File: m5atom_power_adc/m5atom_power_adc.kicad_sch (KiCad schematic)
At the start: 125 parts, among them J1 Conn_01x04_Socket, J10 Relay2, J11 R0SW, J12 R1SW, J13 R2SW, J14 Conn_01x02, J2 GROVE-CONNECTOR, J3 Conn_01x04_Pin, J4 USB_C_Receptacle_USB2.0_16P, J5 SubBatt, J6 MainBatt, J7 Relay0, J8 Relay1, J9 GROVE-CONNECTOR, Q1 AO3401A, Q2 MMBT2222A, Q3 MMBT2222A, Q4 MMBT2222A, Q5 AO3401A, Q6 MMBT2222A, Q7 MMBT2222A, Q8 AO3401A, Q9 MMBT2222A, SW1 Boot, SW2 Reset, U1 LM2596S-5, U2 ESP32-S3-MINI-1, U3 AMS1117-3.3, U4 ADS1115IDGS, U5 AMS1117-3.3, U6 LTC2944

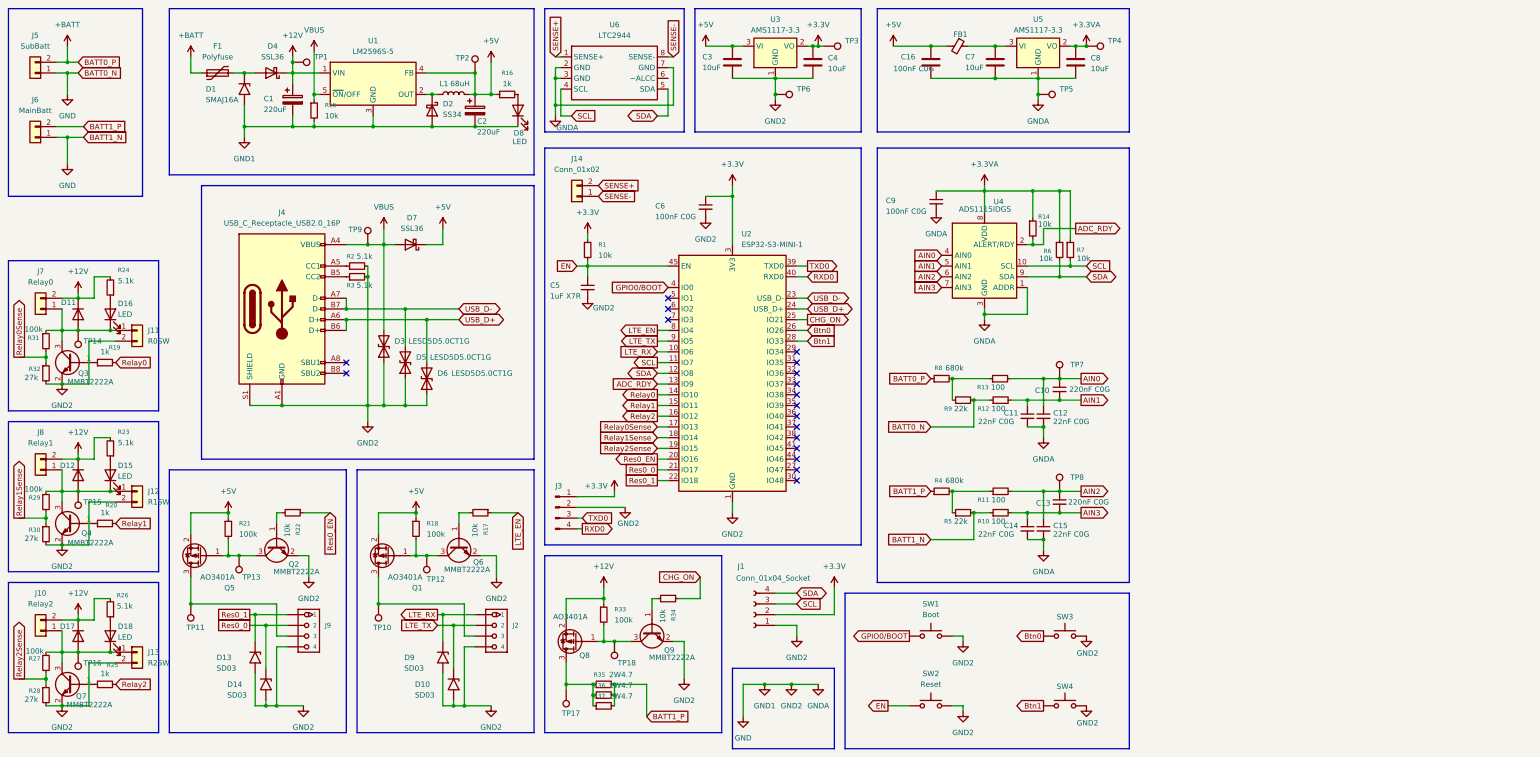
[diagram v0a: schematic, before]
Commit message: refactor: 回路図をフラットから階層化に移行、ブザー回路追加
- 回路図: フラット構成から階層シート構成へ移行（共通回路の共通化）
  - メインシート（1xx）: 電源・ESP32・ADC・ブザー等トップレベル
  - RelayControl サブシート: リレードライバ回路（Q×2、D×3、R×6）
  - VoltageSense サブシート: 電圧分圧回路（C×4、R×5）
  - GroveUnit サブシート: Grove 電源スイッチ回路（Q×3、D×3、R×3）
- 回路図: リファレンス番号をページ番号+xx体系に変更
- 回路図: ブザー回路追加（LS101/MLT-8530 + Q103/AO3401A ハイサイドスイッチ、GPIO34）
- HARDWARE.md: ブザー回路仕様を追記（駆動条件・部品表）
- HARDWARE.md: 赤色LED選定（XL-1608SURC-06）追記
- HARDWARE.md: 電源系統別トレース幅・ビアサイズ表を拡充
- HARDWARE.md: LM2596スイッチングノードの配線注意事項を追記

Co-Authored-By: Claude Sonnet 4.6 <noreply@anthropic.com>
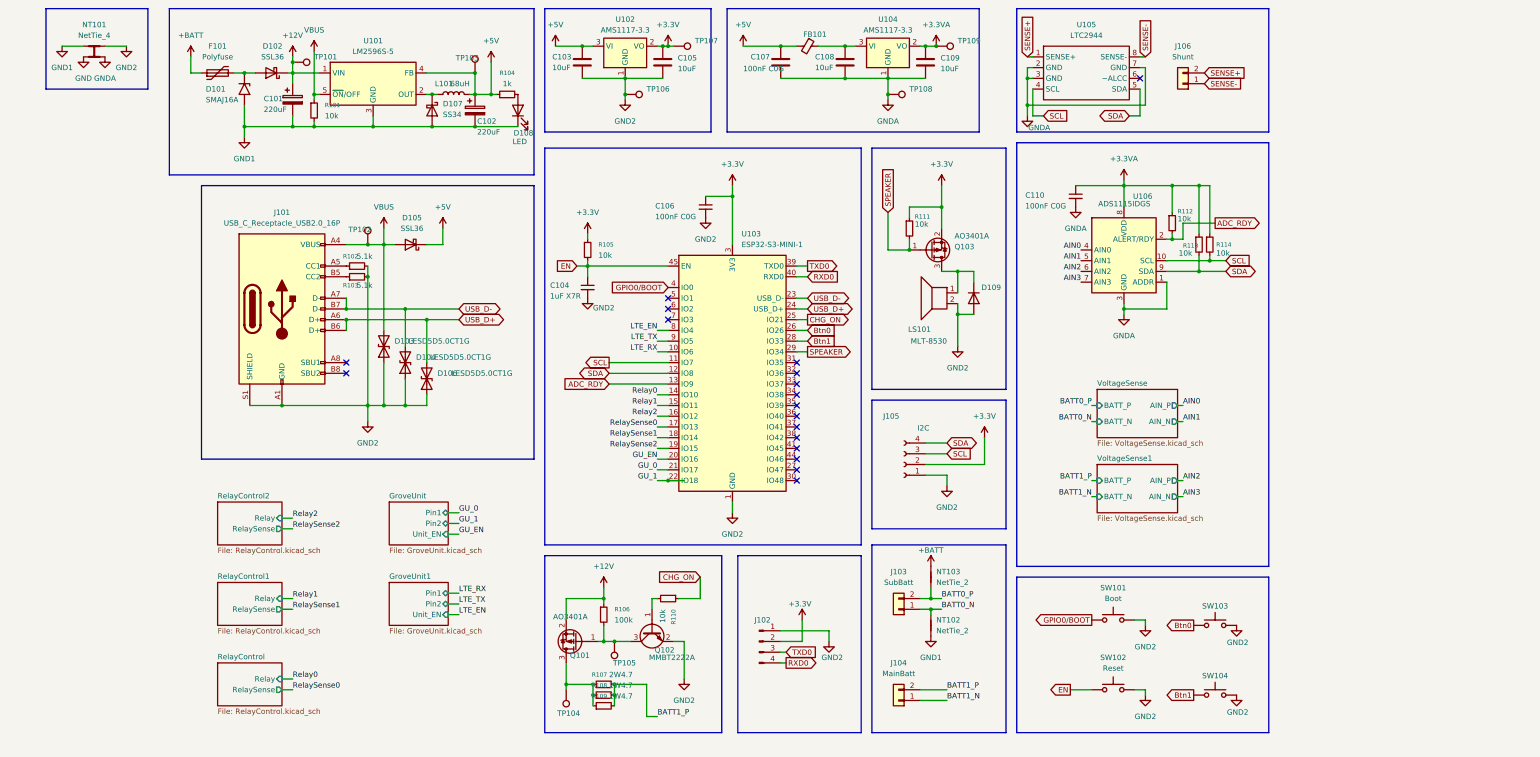
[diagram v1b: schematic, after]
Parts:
- removed C10, C13: 220nF C0G, Capacitor_SMD:C_1206_3216Metric, symbol Device:C_Small
- removed C11, C12, C14, C15: 22nF C0G, Capacitor_SMD:C_0805_2012Metric, symbol Device:C_Small
- removed D10, D13, D14, D9: SD03, Diode_SMD:D_SOD-323, symbol Diode:SMAJ16A
- removed D11, D12, D17: 1N4148WS, Diode_SMD:D_SOD-323, symbol Diode:1N4148WS
- removed D15, D16, D18: LED, LED_SMD:LED_0603_1608Metric, symbol Device:LED
- removed J10: Relay2, Connector_JST:JST_XH_B2B-XH-A_1x02_P2.50mm_Vertical, symbol Connector_Generic:Conn_01x02
- removed J11: R0SW, Connector_JST:JST_XH_B2B-XH-A_1x02_P2.50mm_Vertical, symbol Connector_Generic:Conn_01x02
- removed J12: R1SW, Connector_JST:JST_XH_B2B-XH-A_1x02_P2.50mm_Vertical, symbol Connector_Generic:Conn_01x02
- removed J13: R2SW, Connector_JST:JST_XH_B2B-XH-A_1x02_P2.50mm_Vertical, symbol Connector_Generic:Conn_01x02
- removed J2, J9: GROVE-CONNECTOR, 000_Local:HY2.0-4PWB, symbol OPL_Connector:GROVE-CONNECTOR-DIP_4P-2.0_
- removed J7: Relay0, Connector_JST:JST_XH_B2B-XH-A_1x02_P2.50mm_Vertical, symbol Connector_Generic:Conn_01x02
- removed J8: Relay1, Connector_JST:JST_XH_B2B-XH-A_1x02_P2.50mm_Vertical, symbol Connector_Generic:Conn_01x02
- removed Q1, Q5: AO3401A, Package_TO_SOT_SMD:SOT-23, symbol Transistor_FET:AO3401A
- removed Q2, Q3, Q4, Q6, Q7: MMBT2222A, Package_TO_SOT_SMD:SOT-23, symbol Transistor_BJT:MMBT2222A
- removed R10, R11, R12, R13: 100, Resistor_SMD:R_0402_1005Metric, symbol Device:R_Small
- removed R17, R22: 10k, Resistor_SMD:R_0402_1005Metric, symbol Device:R_Small
- removed R18, R21, R27, R29, R31: 100k, Resistor_SMD:R_0603_1608Metric, symbol Device:R_Small
- removed R19, R20, R25: 1k, Resistor_SMD:R_0603_1608Metric, symbol Device:R_Small
- removed R23, R24, R26: 5.1k, Resistor_SMD:R_0603_1608Metric, symbol Device:R_Small
- removed R28, R30, R32: 27k, Resistor_SMD:R_0603_1608Metric, symbol Device:R_Small
- removed R4, R8: 680k, Resistor_SMD:R_0603_1608Metric, symbol Device:R_Small
- removed R5, R9: 22k, Resistor_SMD:R_0402_1005Metric, symbol Device:R_Small
- removed TP10, TP11, TP12, TP13, TP14, TP15, TP16, TP7, TP8: TestPoint, TestPoint:TestPoint_Pad_D1.5mm, symbol Connector:TestPoint
- added D109: 1N4148WS, Diode_SMD:D_SOD-323, symbol Diode:1N4148WS
- added LS101: MLT-8530, 000_Local:MLT-8530, symbol Device:Speaker
- added NT101: NetTie_4, symbol Device:NetTie_4
- added NT102, NT103: NetTie_2, symbol Device:NetTie_2
- added Q103: AO3401A, Package_TO_SOT_SMD:SOT-23, symbol Transistor_FET:AO3401A
- added R111: 10k, Resistor_SMD:R_0402_1005Metric, symbol Device:R_Small
- F101: renamed from F1; footprint Diode_SMD:D_SMB -> Fuse:Fuse_1812_4532Metric; JLC_Num C19077571 -> C18198333
- J105: renamed from J1; value Conn_01x04_Socket -> I2C
- J106: renamed from J14; value Conn_01x02 -> Shunt
- SW101: renamed from SW1; footprint (none) -> Button_Switch_SMD:SW_SPST_PTS810; JLC_Num (none) -> C221897
- SW102: renamed from SW2; footprint (none) -> Button_Switch_SMD:SW_SPST_PTS810; JLC_Num (none) -> C221897
- SW103: renamed from SW3; footprint (none) -> Button_Switch_SMD:SW_SPST_PTS810; JLC_Num (none) -> C221895
- SW104: renamed from SW4; footprint (none) -> Button_Switch_SMD:SW_SPST_PTS810; JLC_Num (none) -> C221895
- U101: renamed from U1; JLC_Num (none) -> C5349985
- U102: renamed from U3; JLC_Num (none) -> C6186
- U103: renamed from U2; JLC_Num (none) -> C2913206
- U104: renamed from U5; JLC_Num (none) -> C6186
- U106: renamed from U4; JLC_Num (none) -> C2651328
- renumbered C1 to C101, C2 to C102, C3 to C103, C5 to C104, C4 to C105, C6 to C106, C16 to C107, C7 to C108, C8 to C109, C9 to C110, D1 to D101, D4 to D102, D3 to D103, D5 to D104, D7 to D105, D6 to D106, D2 to D107, D8 to D108, FB1 to FB101, J4 to J101, J3 to J102, J5 to J103, J6 to J104, L1 to L101, Q8 to Q101, Q9 to Q102, R15 to R101, R2 to R102, R3 to R103, R16 to R104, R1 to R105, R33 to R106, R35 to R107, R36 to R108, R37 to R109, R34 to R110, R14 to R112, R6 to R113, R7 to R114, TP1 to TP101, TP9 to TP102, TP2 to TP103, TP17 to TP104, TP18 to TP105, TP6 to TP106, TP3 to TP107, TP5 to TP108, TP4 to TP109, U6 to U105
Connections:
- net +3.3V: now also J102.2 (Pin_2), Q103.2 (S), R111.1; no longer J102.1 (Pin_1)
- net +BATT: now also NT103.2; no longer J103.2 (Pin_2)
- net GND: now also NT101.3; no longer C101.2, C102.2, C103.2, C104.2, C105.2, C106.2, C107.2, C108.2, C109.2, C110.2, D101.2 (A2), D103.1 (A1), D104.1 (A1), D106.1 (A1), D107.2 (A), D108.1 (K), J101.A1 (GND), J101.A12 (GND), J101.B1 (GND), J101.B12 (GND), J101.S1 (SHIELD), J102.2 (Pin_2), J103.1 (Pin_1), J104.1 (Pin_1), J105.1 (Pin_1), Q102.2 (E), R101.2, R102.2, R103.2, SW101.2, SW102.2, SW103.2, SW104.2, TP106.1, TP108.1, U101.3 (GND), U102.1 (GND), U103.1 (GND), U103.2 (GND), U103.42 (GND), U103.43 (GND), U103.46 (GND), U103.47 (GND), U103.48 (GND), U103.49 (GND), U103.50 (GND), U103.51 (GND), U103.52 (GND), U103.53 (GND), U103.54 (GND), U103.55 (GND), U103.56 (GND), U103.57 (GND), U103.58 (GND), U103.59 (GND), U103.60 (GND), U103.61 (GND), U103.62 (GND), U103.63 (GND), U103.64 (GND), U103.65 (GND), U104.1 (GND), U105.2 (GND), U105.3 (GND), U105.7 (GND), U106.1 (ADDR), U106.3 (GND)
- net SPEAKER: now reaches U103.29 (IO34)
- net SPEAKER: now also Q103.1 (G), R111.2
- net Relay0Sense renamed RelaySense0
- net Relay1Sense renamed RelaySense1
- net Relay2Sense renamed RelaySense2
- net Res0_0 renamed GU_0
- net Res0_1 renamed GU_1
- net Res0_EN renamed GU_EN
- new net: D109.1 (K), LS101.1, Q103.3 (D)
- new net BATT0_N: J103.1 (Pin_1), NT102.2
- new net BATT0_P: J103.2 (Pin_2), NT103.1
- new net BATT1_N: J104.1 (Pin_1)
- new net GND1: C101.2, C102.2, D101.2 (A2), D107.2 (A), D108.1 (K), NT101.1, NT102.1, R101.2, U101.3 (GND)
- new net GND2: C103.2, C104.2, C105.2, C106.2, D103.1 (A1), D104.1 (A1), D106.1 (A1), D109.2 (A), J101.A1 (GND), J101.A12 (GND), J101.B1 (GND), J101.B12 (GND), J101.S1 (SHIELD), J102.1 (Pin_1), J105.1 (Pin_1), LS101.2, NT101.2, Q102.2 (E), R102.2, R103.2, SW101.2, SW102.2, SW103.2, SW104.2, TP106.1, U102.1 (GND), U103.1 (GND), U103.2 (GND), U103.42 (GND), U103.43 (GND), U103.46 (GND), U103.47 (GND), U103.48 (GND), U103.49 (GND), U103.50 (GND), U103.51 (GND), U103.52 (GND), U103.53 (GND), U103.54 (GND), U103.55 (GND), U103.56 (GND), U103.57 (GND), U103.58 (GND), U103.59 (GND), U103.60 (GND), U103.61 (GND), U103.62 (GND), U103.63 (GND), U103.64 (GND), U103.65 (GND)
- new net GNDA: C107.2, C108.2, C109.2, C110.2, NT101.4, TP108.1, U104.1 (GND), U105.2 (GND), U105.3 (GND), U105.7 (GND), U106.1 (ADDR), U106.3 (GND)
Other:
- added sheet GroveUnit (GroveUnit.kicad_sch)
- added sheet GroveUnit1 (GroveUnit.kicad_sch)
- added sheet RelayControl (RelayControl.kicad_sch)
- added sheet RelayControl1 (RelayControl.kicad_sch)
- added sheet RelayControl2 (RelayControl.kicad_sch)
- added sheet VoltageSense (VoltageSense.kicad_sch)
- added sheet VoltageSense1 (VoltageSense.kicad_sch)
- moved on the sheet: C103, C105, C107, C108, C109, C110, FB101, J102, J103, J104, J105, J106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

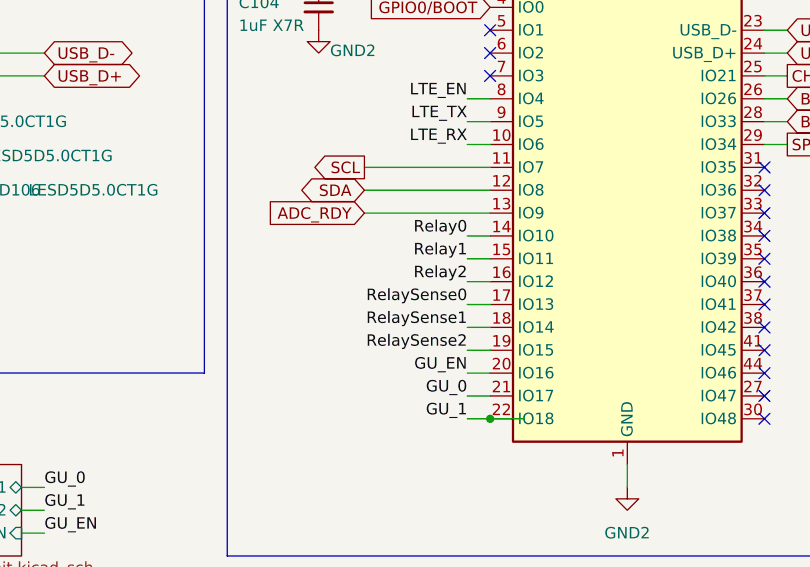
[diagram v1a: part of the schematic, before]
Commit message: fix: PCBレイアウトに合わせて回路図・PCBを微修正
Co-Authored-By: Claude Sonnet 4.6 <noreply@anthropic.com>
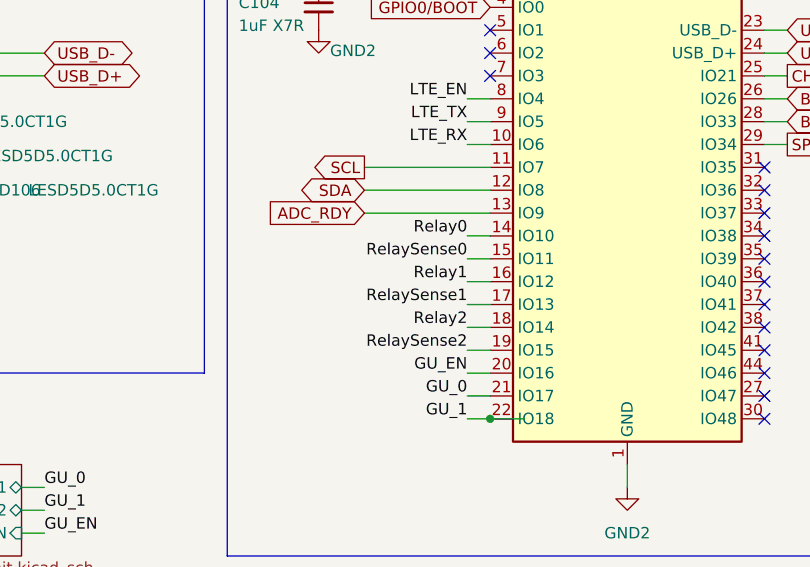
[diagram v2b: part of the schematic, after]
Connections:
- net Relay1: now also U103.16 (IO12); no longer U103.15 (IO11)
- net Relay2: now also U103.18 (IO14); no longer U103.16 (IO12)
- net RelaySense0: now also U103.15 (IO11); no longer U103.17 (IO13)
- net RelaySense1: now also U103.17 (IO13); no longer U103.18 (IO14)
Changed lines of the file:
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@@
 	(wire
 		(pts
-			(xy 167.64 120.65) (xy 170.18 120.65)
-		)
-		(stroke
-			(width 0)
-			(type default)
-		)
-	)
-	(wire
-		(pts
 			(xy 154.94 161.29) (xy 154.94 162.56)
 		)
@@
 	(wire
 		(pts
-			(xy 160.02 38.1) (xy 168.91 38.1)
+			(xy 167.64 120.65) (xy 170.18 120.65)
 		)
 		(stroke
@@
 	(wire
 		(pts
-			(xy 167.64 128.27) (xy 170.18 128.27)
+			(xy 167.64 115.57) (xy 170.18 115.57)
 		)
 		(stroke
@@
 	(wire
 		(pts
-			(xy 280.67 182.88) (xy 283.21 182.88)
+			(xy 160.02 38.1) (xy 168.91 38.1)
 		)
 		(stroke
@@
 	(wire
 		(pts
-			(xy 167.64 115.57) (xy 170.18 115.57)
+			(xy 167.64 128.27) (xy 170.18 128.27)
+		)
+		(stroke
+			(width 0)
+			(type default)
+		)
+	)
+	(wire
+		(pts
+			(xy 280.67 182.88) (xy 283.21 182.88)
 		)
 		(stroke
@@
 	(wire
 		(pts
+			(xy 167.64 123.19) (xy 170.18 123.19)
+		)
+		(stroke
+			(width 0)
+			(type default)
+		)
+	)
+	(wire
+		(pts
 			(xy 229.87 185.42) (xy 236.22 185.42)
 		)
@@
 	(wire
 		(pts
-			(xy 167.64 118.11) (xy 170.18 118.11)
-		)
-		(stroke
-			(width 0)
-			(type default)
-		)
-	)
-	(wire
-		(pts
 			(xy 255.27 35.56) (xy 255.27 38.1)
 		)
@@
 	(wire
 		(pts
-			(xy 167.64 123.19) (xy 170.18 123.19)
+			(xy 160.02 41.91) (xy 160.02 43.18)
 		)
 		(stroke
@@
 	(wire
 		(pts
-			(xy 160.02 41.91) (xy 160.02 43.18)
+			(xy 203.2 82.55) (xy 200.66 82.55)
 		)
 		(stroke
@@
 	(wire
 		(pts
-			(xy 203.2 82.55) (xy 200.66 82.55)
+			(xy 212.09 30.48) (xy 214.63 30.48)
 		)
 		(stroke
@@
 	(wire
 		(pts
-			(xy 212.09 30.48) (xy 214.63 30.48)
+			(xy 86.36 49.53) (xy 100.33 49.53)
 		)
 		(stroke
@@
 	(wire
 		(pts
-			(xy 86.36 49.53) (xy 100.33 49.53)
+			(xy 81.28 49.53) (xy 86.36 49.53)
 		)
 		(stroke
@@
 	(wire
 		(pts
-			(xy 81.28 49.53) (xy 86.36 49.53)
+			(xy 167.64 113.03) (xy 170.18 113.03)
 		)
 		(stroke
@@
 	(wire
 		(pts
+			(xy 167.64 125.73) (xy 170.18 125.73)
+		)
+		(stroke
+			(width 0)
+			(type default)
+		)
+	)
+	(wire
+		(pts
 			(xy 86.36 41.91) (xy 87.63 41.91)
 		)
@@
 	(wire
 		(pts
+			(xy 167.64 118.11) (xy 170.18 118.11)
+		)
+		(stroke
+			(width 0)
+			(type default)
+		)
+	)
+	(wire
+		(pts
 			(xy 102.87 115.57) (xy 107.95 115.57)
 		)
@@
 	(wire
 		(pts
-			(xy 167.64 125.73) (xy 170.18 125.73)
-		)
-		(stroke
-			(width 0)
-			(type default)
-		)
-	)
-	(wire
-		(pts
 			(xy 238.76 91.44) (xy 238.76 93.98)
 		)
@@
 	(wire
 		(pts
-			(xy 167.64 113.03) (xy 170.18 113.03)
-		)
-		(stroke
-			(width 0)
-			(type default)
-		)
-	)
-	(wire
-		(pts
 			(xy 229.87 182.88) (xy 236.22 182.88)
 		)
@@
 	)
 	(label "RelaySense0"
-		(at 167.64 120.65 180)
+		(at 167.64 115.57 180)
 		(effects
 			(font
@@
 	)
 	(label "Relay1"
-		(at 167.64 115.57 180)
+		(at 167.64 118.11 180)
 		(effects
 			(font
@@
 	)
 	(label "Relay2"
-		(at 167.64 118.11 180)
+		(at 167.64 123.19 180)
 		(effects
 			(font
@@
 	)
 	(label "RelaySense1"
-		(at 167.64 123.19 180)
+		(at 167.64 120.65 180)
 		(effects
 			(font
